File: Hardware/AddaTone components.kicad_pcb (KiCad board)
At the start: 2 copper layers, 60 x 110 mm, 86 parts, among them J1 SWD_Header, J2 Conn_01x10_Female, J3 Conn_01x12_Female, J4 Conn_01x03_Male, J5 Conn_01x06_Male, J6 Conn_01x03_Male, J8 Eurorack_16_pin_power, U1 STM32F446RETx, U2 ICE40UP5K-SG48ITR, U3 MCP6004, U4 PCM5100APW, U5 TL072, U6 LD1117S12TR, U7 LM1117-3.3, Y1 ECS-12MHz

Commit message: Refinements to PCB
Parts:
- added J7: Conn_01x02_Male, Pin_Headers:Pin_Header_Straight_1x02_Pitch2.54mm, F.Cu at (116.7, 142.0)
- added TP2: TestPoint, Pin_Headers:Pin_Header_Straight_1x01_Pitch2.54mm, F.Cu at (136.4, 74.5)
- added TP3: TestPoint, Pin_Headers:Pin_Header_Straight_1x01_Pitch2.54mm, F.Cu at (106.1, 155.6)
- added TP4: TestPoint, Pin_Headers:Pin_Header_Straight_1x01_Pitch2.54mm, F.Cu at (131.2, 67.6)
- added TP5: TestPoint, Pin_Headers:Pin_Header_Straight_1x01_Pitch2.54mm, F.Cu at (136.2, 84.3)
- added TP6: TestPoint, Pin_Headers:Pin_Header_Straight_1x01_Pitch2.54mm, F.Cu at (144.7, 84.2)
- added TP7: TestPoint, Measurement_Points:Test_Point_Keystone_5010-5014_Multipurpose, F.Cu at (103.7, 151.1)
- TP1: footprint Socket_Strips:Socket_Strip_Straight_1x01_Pitch2.54mm -> Pin_Headers:Pin_Header_Straight_1x01_Pitch2.54mm
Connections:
- U2 pad 42: Net-(U2-Pad42) -> F_TEST1
- U2 pad 45: Net-(U2-Pad45) -> F_TEST2
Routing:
- net +3.3VA: track 208.6 -> 216.6 mm
- net +1V2: track 68.7 -> 76.6 mm
- net VCC: track 150.9 -> 157.8 mm
- net VEE: track 120.7 -> 126.2 mm
- net VCCIO_0: track 319.8 -> 324.5 mm
- net F_TEST1: track 0.00 -> 4.33 mm
- net F_TEST2: track 0.00 -> 4.30 mm
- net GND: vias 40 -> 45
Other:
- board text added: "+12V"
- board text added: "-12V"
- board text added: "1 TST 2"
- board text added: "1V2"
- board text added: "3V3"
- board text added: "Addatone v1.0 Mountjoy Modular"
- board text added: "FPGA PRG"
- board text added: "MCO"

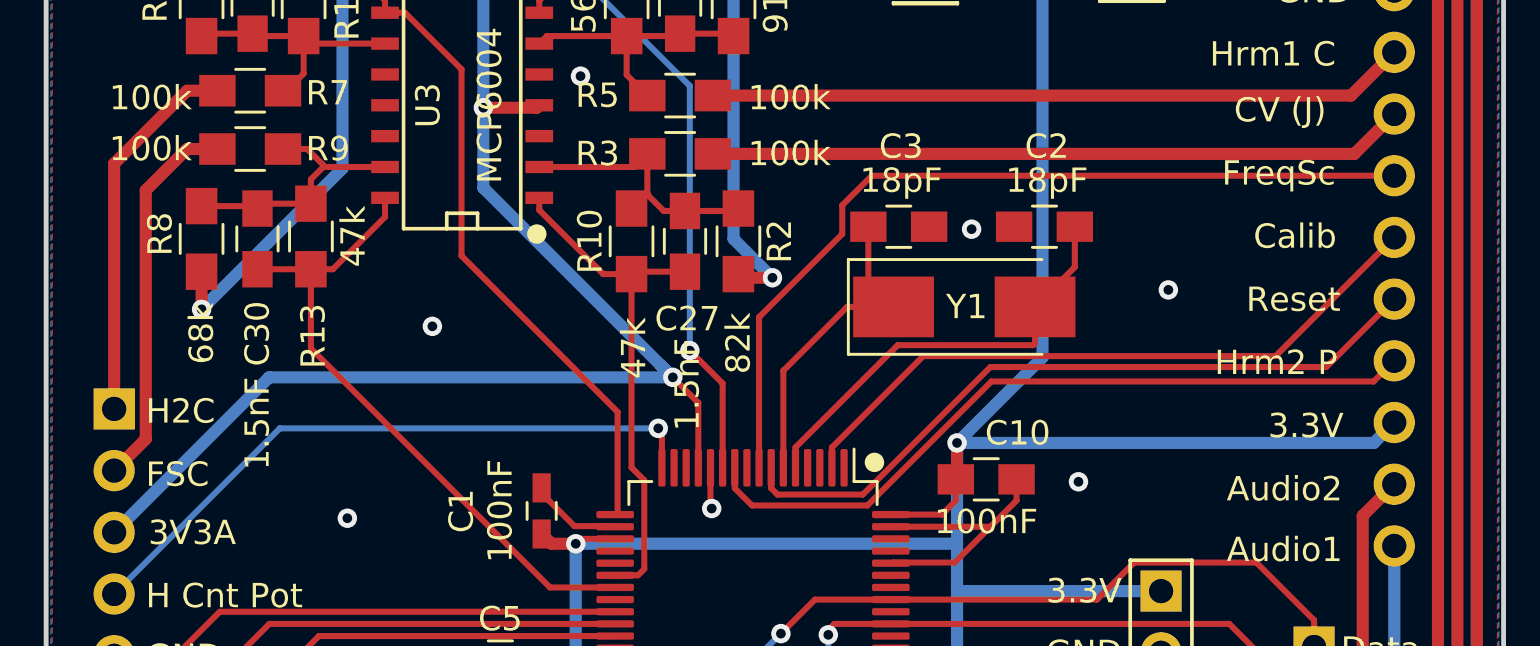
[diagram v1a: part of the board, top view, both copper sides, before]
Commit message: Updated FPGA programming code to use correct pin for Reset; Minor PCB corrections
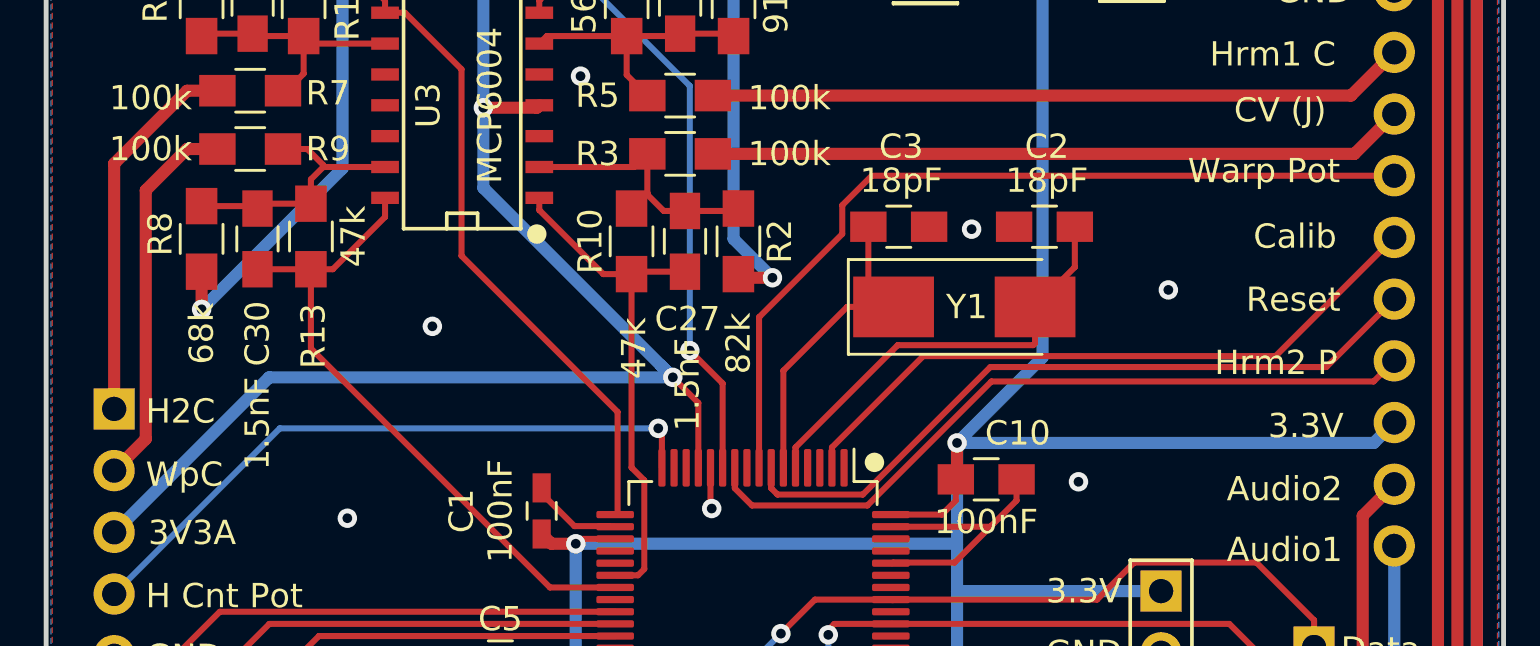
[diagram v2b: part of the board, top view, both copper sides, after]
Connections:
- net FREQ_SCALE_CV renamed WARP_CV
- net FREQ_SCALE_CVIN renamed WARP_CVIN
- net FREQ_SC_POT renamed WARP_POT
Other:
- board text added: "Warp Pot"
- board text added: "WpC"
- board text removed: "FSC"
- board text removed: "FreqSc"

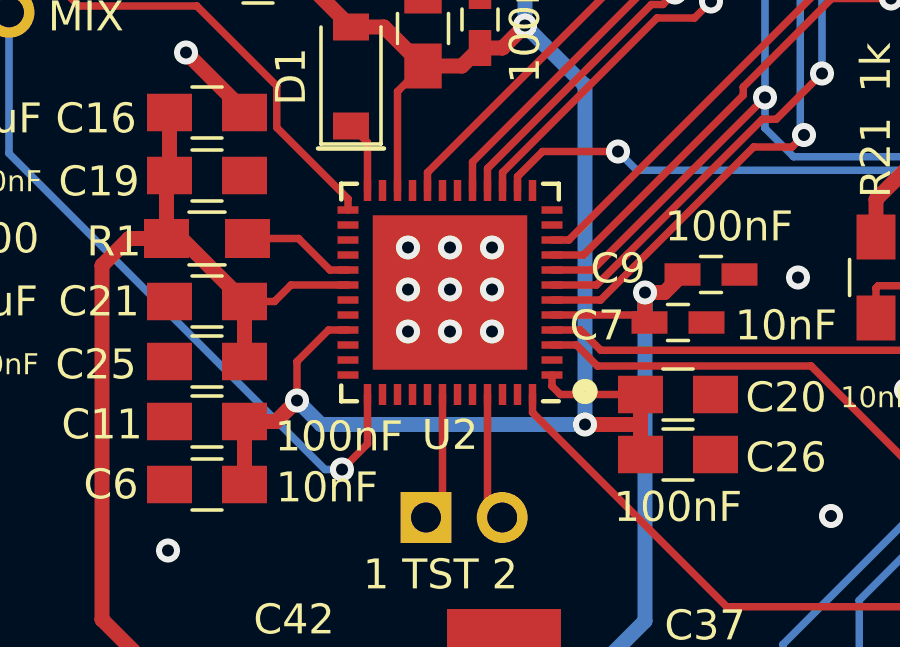
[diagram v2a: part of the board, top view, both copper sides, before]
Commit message: Switched FPGA output to I2S DAC
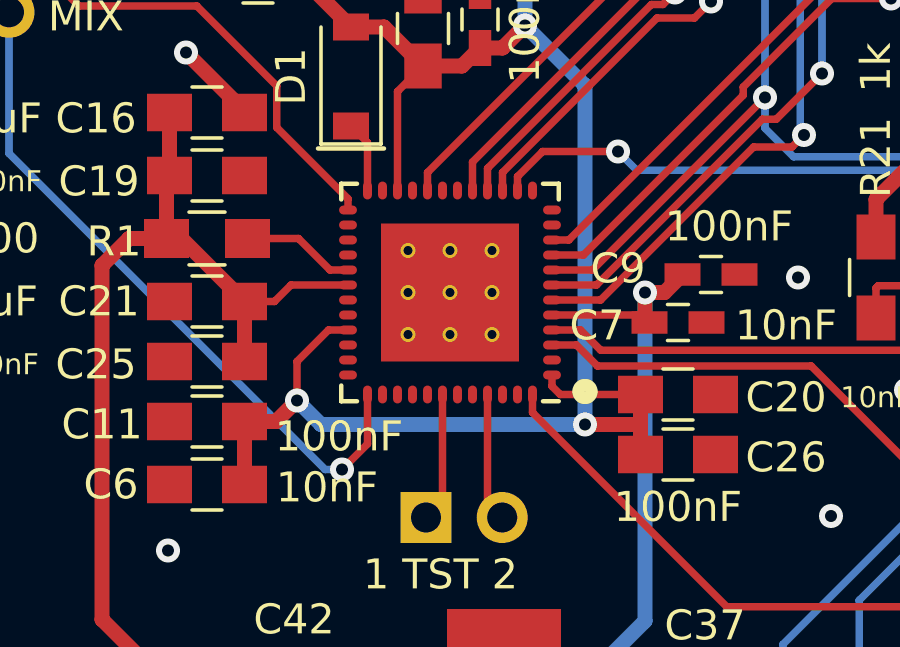
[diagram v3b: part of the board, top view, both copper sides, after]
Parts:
- U2: footprint Housings_DFN_QFN:QFN-48-1EP_7x7mm_Pitch0.5mm -> Custom_Footprints:ICE40_QFN-48-1EP_7x7mm_Pitch0.5mm
- turned U2 to 270 degrees
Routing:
- net GND: vias 45 -> 36

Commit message: Updates to PCB layout
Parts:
- J2, J3: moved to B.Cu
- moved Y1 3.16 mm to (135.2, 99.9)
- moved C2 3.16 mm to (138.5, 96.6)
- moved C3 3.16 mm to (132.5, 96.6)
- moved C35 0.20 mm to (135.4, 146.7)
- turned J2 to 180 degrees
- turned J3 to 180 degrees
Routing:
- net GND: track 65.5 -> 59.8 mm, vias 36 -> 42
- net Net-(C3-Pad1): track 13.4 -> 9.77 mm
- net Net-(C2-Pad1): track 18.0 -> 14.5 mm
- net WARP_POT: track 35.5 -> 37.0 mm
- net VCCIO_0: track 324.5 -> 323.2 mm
- net ADC_Data: track 54.2 -> 53.1 mm
- net Net-(C30-Pad1): track 10.9 -> 11.8 mm
- net WARP_CV: track 26.9 -> 27.8 mm
- net +3.3VA: track 216.6 -> 217.3 mm
- net AREF_-5: track 67.2 -> 67.9 mm
- net MCO2_CLOCK_OUT: track 22.5 -> 21.9 mm
- net FPGA_SCK: track 36.8 -> 37.4 mm

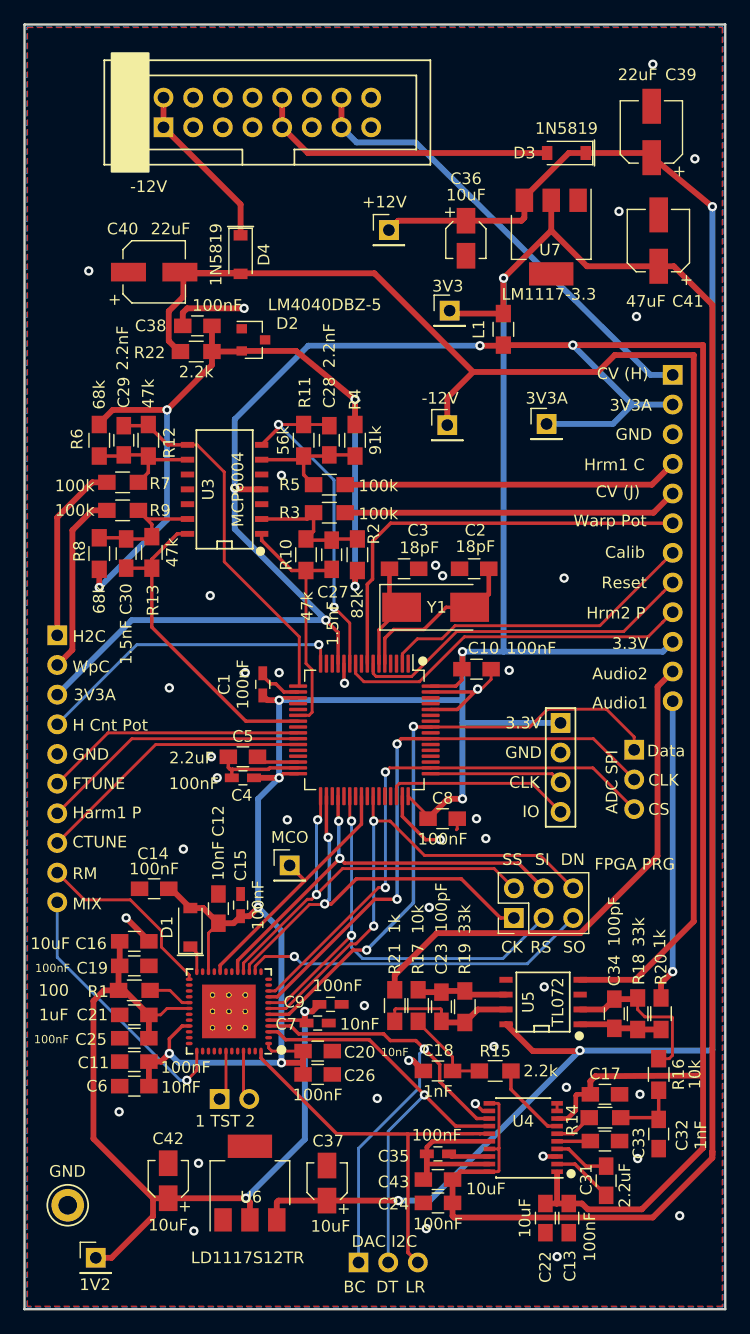
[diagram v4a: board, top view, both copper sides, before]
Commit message: Fixes to schematic (missing resistor on 1.2V LDO); Created new implementation to support production board; added FPGA tester project
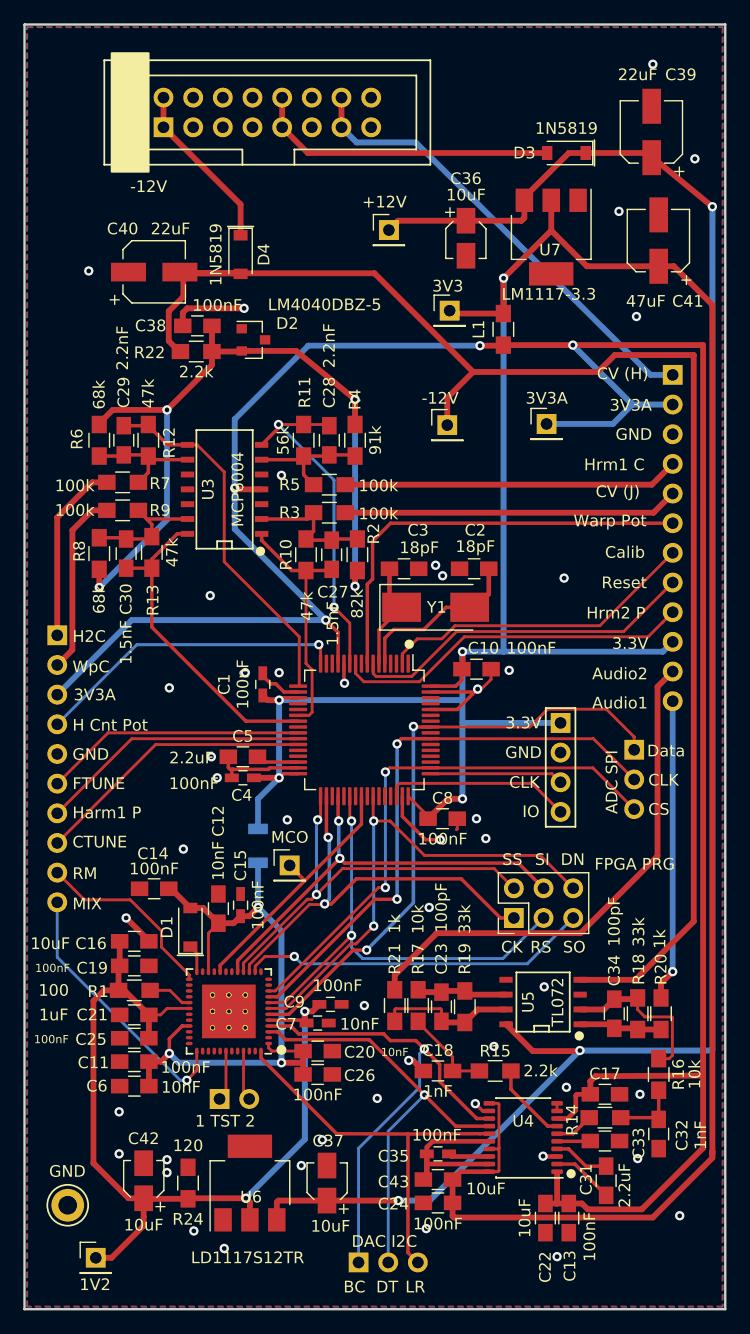
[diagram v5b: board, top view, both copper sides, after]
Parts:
- added R23: 0, Resistors_SMD:R_1206, B.Cu at (120.0, 120.3)
- added R24: 120, Resistors_SMD:R_0805_HandSoldering, F.Cu at (114.0, 149.2)
- U4: footprint Housings_SSOP:SSOP-20_4.4x6.5mm_Pitch0.65mm -> Custom_Footprints:SSOP-20_4.4x6.5mm_Pitch0.65mm_Round_Pads
- moved C42 2.10 mm to (110.2, 149.0)
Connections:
- C1 pad 1: VCCIO_0 -> +3V3
- C10 pad 1: VCCIO_0 -> +3V3
- C24 pad 1: VCCIO_0 -> +3V3
- C4 pad 1: VCCIO_0 -> +3V3
- C41 pad 1: VCCIO_0 -> +3V3
- C43 pad 1: VCCIO_0 -> +3V3
- C8 pad 1: VCCIO_0 -> +3V3
- J1 pad 1: VCCIO_0 -> +3V3
- J3 pad 10: VCCIO_0 -> +3V3
- L1 pad 2: VCCIO_0 -> +3V3
- TP2 pad 1: VCCIO_0 -> +3V3
- U1 pad 19: VCCIO_0 -> +3V3
- U1 pad 32: VCCIO_0 -> +3V3
- U1 pad 48: VCCIO_0 -> +3V3
- U1 pad 64: VCCIO_0 -> +3V3
- U4 pad 11: VCCIO_0 -> +3V3
- U4 pad 17: VCCIO_0 -> +3V3
- U4 pad 20: VCCIO_0 -> +3V3
- U7 pad 2: VCCIO_0 -> +3V3
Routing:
- net VCCIO_0: track 323.2 -> 57.0 mm, vias 8 -> 3
- net +3V3: track 0.00 -> 263.3 mm, vias 0 -> 5
- net +1V2: track 76.6 -> 77.6 mm
- net GND: vias 42 -> 47
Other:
- board text added: "Addatone v2.0 Mountjoy Modular"
- board text added: "FPGA 3V3"
- board text removed: "Addatone v1.0 Mountjoy Modular"

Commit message: Updated pcb files to Kicad 6.0
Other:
- net class Default removed
- net class Wide_Power removed
